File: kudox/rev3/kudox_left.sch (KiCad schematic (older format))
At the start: 72 parts, among them K0 KEYSW, K1 KEYSW, K10 KEYSW, K11 KEYSW, K12 KEYSW, K13 KEYSW, K14 KEYSW, K15 KEYSW, K16 KEYSW, K2 KEYSW, K20 KEYSW, K21 KEYSW, K22 KEYSW, K23 KEYSW, K24 KEYSW, K25 KEYSW, K3 KEYSW, K30 KEYSW, K31 KEYSW, K32 KEYSW, K33 KEYSW, K34 KEYSW, K35 KEYSW, K4 KEYSW, K40 KEYSW, K41 KEYSW, K42 KEYSW, K43 KEYSW, K44 KEYSW, K45 KEYSW, K46 KEYSW, K5 KEYSW, K6 KEYSW, U1 ProMicro

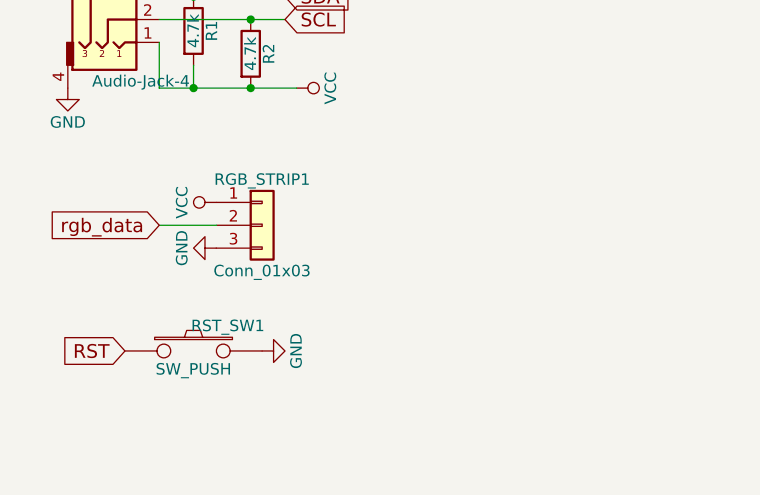
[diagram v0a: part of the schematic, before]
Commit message: Modify kudox/rev3 to add RGB pad
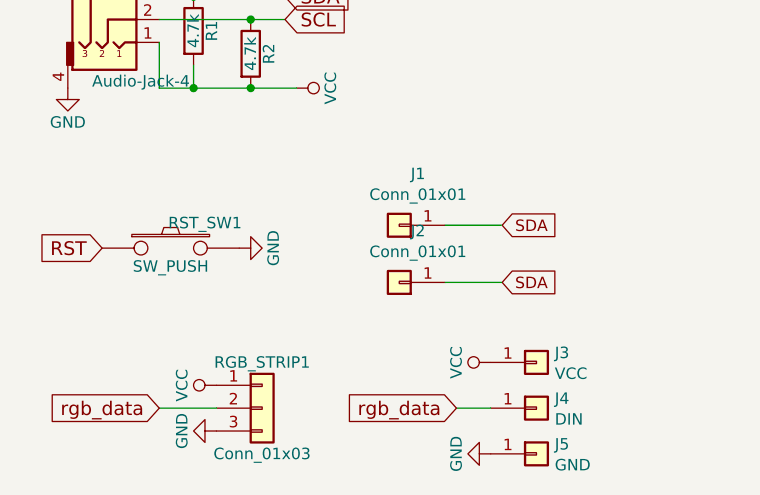
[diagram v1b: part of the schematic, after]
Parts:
- added J1: Conn_01x01, kudox_footprints:Pin_Header_Straight_1x01_Pitch2.54mm, symbol Connector_Generic:Conn_01x01
- added J2: Conn_01x01, kudox_footprints:rgb_pad, symbol Connector_Generic:Conn_01x01
- added J3: VCC, kudox_footprints:pad_1x1, symbol Connector_Generic:Conn_01x01
- added J4: DIN, kudox_footprints:pad_1x1, symbol Connector_Generic:Conn_01x01
- added J5: GND, kudox_footprints:pad_1x1, symbol Connector_Generic:Conn_01x01
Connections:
- net GND: now also J5.1 (Pin_1)
- net SDA: now also J1.1 (Pin_1), J2.1 (Pin_1)
- net VCC: now also J3.1 (Pin_1)
- net rgb_data: now also J4.1 (Pin_1)
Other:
- moved on the sheet: RGB_STRIP1, RST_SW1
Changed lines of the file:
@@
 EESchema Schematic File Version 4
-LIBS:kudox_left-cache
-EELAYER 29 0
+EELAYER 30 0
 EELAYER END
 $Descr A4 11693 8268
@@
 Sheet 1 1
 Title "Kudox keyboard"
-Date "2020-01-30"
-Rev "3.0"
+Date "2021-05-01"
+Rev "3.1"
 Comp "Kumao Kobo"
 Comment1 "designed by x1 and inken"
@@
 $EndComp
 $Comp
-L kudox-parts:Conn_01x03 RGB_STRIP1
-U 1 1 5A8088A7
-P 1750 4200
-F 0 "RGB_STRIP1" H 1750 4400 50  0000 C CNN
-F 1 "Conn_01x03" H 1750 4000 50  0000 C CNN
-F 2 "kudox_footprints:Pin_Header_Straight_1x03_Pitch2.54mm" H 1750 4200 50  0001 C CNN
-F 3 "" H 1750 4200 50  0001 C CNN
-	1    1750 4200
-	1    0    0    -1
-$EndComp
-$Comp
 L kudox-parts:SW_PUSH RST_SW1
 U 1 1 5A808917
-P 1450 4750
-F 0 "RST_SW1" H 1600 4860 50  0000 C CNN
-F 1 "SW_PUSH" H 1450 4670 50  0000 C CNN
-F 2 "kudox_footprints:SW_PUSH_6mm_h4.3mm" H 1450 4750 60  0001 C CNN
-F 3 "" H 1450 4750 60  0000 C CNN
-	1    1450 4750
+P 1350 4300
+F 0 "RST_SW1" H 1500 4410 50  0000 C CNN
+F 1 "SW_PUSH" H 1350 4220 50  0000 C CNN
+F 2 "kudox_footprints:SW_PUSH_6mm_h4.3mm" H 1350 4300 60  0001 C CNN
+F 3 "" H 1350 4300 60  0000 C CNN
+	1    1350 4300
 	1    0    0    -1
 $EndComp
@@
 Wire Wire Line
 	1300 3300 1700 3300
-$Comp
-L kudox-parts:GND #PWR04
-U 1 1 5A808EA3
-P 1550 4300
-F 0 "#PWR04" H 1550 4050 50  0001 C CNN
-F 1 "GND" H 1550 4150 50  0000 C CNN
-F 2 "" H 1550 4300 50  0001 C CNN
-F 3 "" H 1550 4300 50  0001 C CNN
-	1    1550 4300
-	0    1    1    0
-$EndComp
-$Comp
-L kudox-parts:VCC #PWR05
-U 1 1 5A808EBA
-P 1550 4100
-F 0 "#PWR05" H 1550 3950 50  0001 C CNN
-F 1 "VCC" H 1550 4250 50  0000 C CNN
-F 2 "" H 1550 4100 50  0001 C CNN
-F 3 "" H 1550 4100 50  0001 C CNN
-	1    1550 4100
-	0    -1   -1   0
-$EndComp
-Text GLabel 1300 4200 0    60   Input ~ 0
-rgb_data
-Wire Wire Line
-	1300 4200 1550 4200
-Text GLabel 1150 4750 0    60   Input ~ 0
+Text GLabel 1050 4300 0    60   Input ~ 0
 RST
 $Comp
 L kudox-parts:GND #PWR06
 U 1 1 5A80901B
-P 1750 4750
-F 0 "#PWR06" H 1750 4500 50  0001 C CNN
-F 1 "GND" H 1750 4600 50  0000 C CNN
-F 2 "" H 1750 4750 50  0001 C CNN
-F 3 "" H 1750 4750 50  0001 C CNN
-	1    1750 4750
+P 1650 4300
+F 0 "#PWR06" H 1650 4050 50  0001 C CNN
+F 1 "GND" H 1650 4150 50  0000 C CNN
+F 2 "" H 1650 4300 50  0001 C CNN
+F 3 "" H 1650 4300 50  0001 C CNN
+	1    1650 4300
 	0    -1   -1   0
 $EndComp
@@
 	8600 1900 9400 1900
 Connection ~ 8600 1900
+$Comp
+L Connector_Generic:Conn_01x01 J1
+U 1 1 605E132A
+P 2350 4200
+F 0 "J1" H 2268 3975 50  0000 C CNN
+F 1 "Conn_01x01" H 2268 4066 50  0000 C CNN
+F 2 "kudox_footprints:Pin_Header_Straight_1x01_Pitch2.54mm" H 2350 4200 50  0001 C CNN
+F 3 "~" H 2350 4200 50  0001 C CNN
+	1    2350 4200
+	-1   0    0    1
+$EndComp
+Text GLabel 2800 4200 2    50   Input ~ 0
+SDA
+Wire Wire Line
+	2550 4200 2800 4200
+$Comp
+L Connector_Generic:Conn_01x01 J2
+U 1 1 60611F0D
+P 2350 4450
+F 0 "J2" H 2268 4225 50  0000 C CNN
+F 1 "Conn_01x01" H 2268 4316 50  0000 C CNN
+F 2 "kudox_footprints:rgb_pad" H 2350 4450 50  0001 C CNN
+F 3 "~" H 2350 4450 50  0001 C CNN
+	1    2350 4450
+	-1   0    0    1
+$EndComp
+Text GLabel 2800 4450 2    50   Input ~ 0
+SDA
+Wire Wire Line
+	2550 4450 2800 4450
+Wire Wire Line
+	1300 5000 1550 5000
+Text GLabel 1300 5000 0    60   Input ~ 0
+rgb_data
+$Comp
+L kudox-parts:VCC #PWR05
+U 1 1 5A808EBA
+P 1550 4900
+F 0 "#PWR05" H 1550 4750 50  0001 C CNN
+F 1 "VCC" H 1550 5050 50  0000 C CNN
+F 2 "" H 1550 4900 50  0001 C CNN
+F 3 "" H 1550 4900 50  0001 C CNN
+	1    1550 4900
+	0    -1   -1   0
+$EndComp
+$Comp
+L kudox-parts:GND #PWR04
+U 1 1 5A808EA3
+P 1550 5100
+F 0 "#PWR04" H 1550 4850 50  0001 C CNN
+F 1 "GND" H 1550 4950 50  0000 C CNN
+F 2 "" H 1550 5100 50  0001 C CNN
+F 3 "" H 1550 5100 50  0001 C CNN
+	1    1550 5100
+	0    1    1    0
+$EndComp
+$Comp
+L kudox-parts:Conn_01x03 RGB_STRIP1
+U 1 1 5A8088A7
+P 1750 5000
+F 0 "RGB_STRIP1" H 1750 5200 50  0000 C CNN
+F 1 "Conn_01x03" H 1750 4800 50  0000 C CNN
+F 2 "kudox_footprints:Pin_Header_Straight_1x03_Pitch2.54mm" H 1750 5000 50  0001 C CNN
+F 3 "" H 1750 5000 50  0001 C CNN
+	1    1750 5000
+	1    0    0    -1
+$EndComp
+Text GLabel 2600 5000 0    60   Input ~ 0
+rgb_data
+$Comp
+L kudox-parts:VCC #PWR0101
+U 1 1 60F2053E
+P 2750 4800
+F 0 "#PWR0101" H 2750 4650 50  0001 C CNN
+F 1 "VCC" H 2750 4950 50  0000 C CNN
+F 2 "" H 2750 4800 50  0001 C CNN
+F 3 "" H 2750 4800 50  0001 C CNN
+	1    2750 4800
+	0    -1   -1   0
+$EndComp
+$Comp
+L kudox-parts:GND #PWR0102
+U 1 1 60F20544
+P 2750 5200
+F 0 "#PWR0102" H 2750 4950 50  0001 C CNN
+F 1 "GND" H 2750 5050 50  0000 C CNN
+F 2 "" H 2750 5200 50  0001 C CNN
+F 3 "" H 2750 5200 50  0001 C CNN
+	1    2750 5200
+	0    1    1    0
+$EndComp
+$Comp
+L Connector_Generic:Conn_01x01 J3
+U 1 1 60F2535A
+P 2950 4800
+F 0 "J3" H 3030 4842 50  0000 L CNN
+F 1 "VCC" H 3030 4751 50  0000 L CNN
+F 2 "kudox_footprints:pad_1x1" H 2950 4800 50  0001 C CNN
+F 3 "~" H 2950 4800 50  0001 C CNN
+	1    2950 4800
+	1    0    0    -1
+$EndComp
+$Comp
+L Connector_Generic:Conn_01x01 J4
+U 1 1 60F254D6
+P 2950 5000
+F 0 "J4" H 3030 5042 50  0000 L CNN
+F 1 "DIN" H 3030 4951 50  0000 L CNN
+F 2 "kudox_footprints:pad_1x1" H 2950 5000 50  0001 C CNN
+F 3 "~" H 2950 5000 50  0001 C CNN
+	1    2950 5000
+	1    0    0    -1
+$EndComp
+$Comp
+L Connector_Generic:Conn_01x01 J5
+U 1 1 60F29E55
+P 2950 5200
+F 0 "J5" H 3030 5242 50  0000 L CNN
+F 1 "GND" H 3030 5151 50  0000 L CNN
+F 2 "kudox_footprints:pad_1x1" H 2950 5200 50  0001 C CNN
+F 3 "~" H 2950 5200 50  0001 C CNN
+	1    2950 5200
+	1    0    0    -1
+$EndComp
+Wire Wire Line
+	2750 5000 2600 5000
 $EndSCHEMATC
